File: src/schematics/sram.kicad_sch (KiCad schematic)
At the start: 4 parts

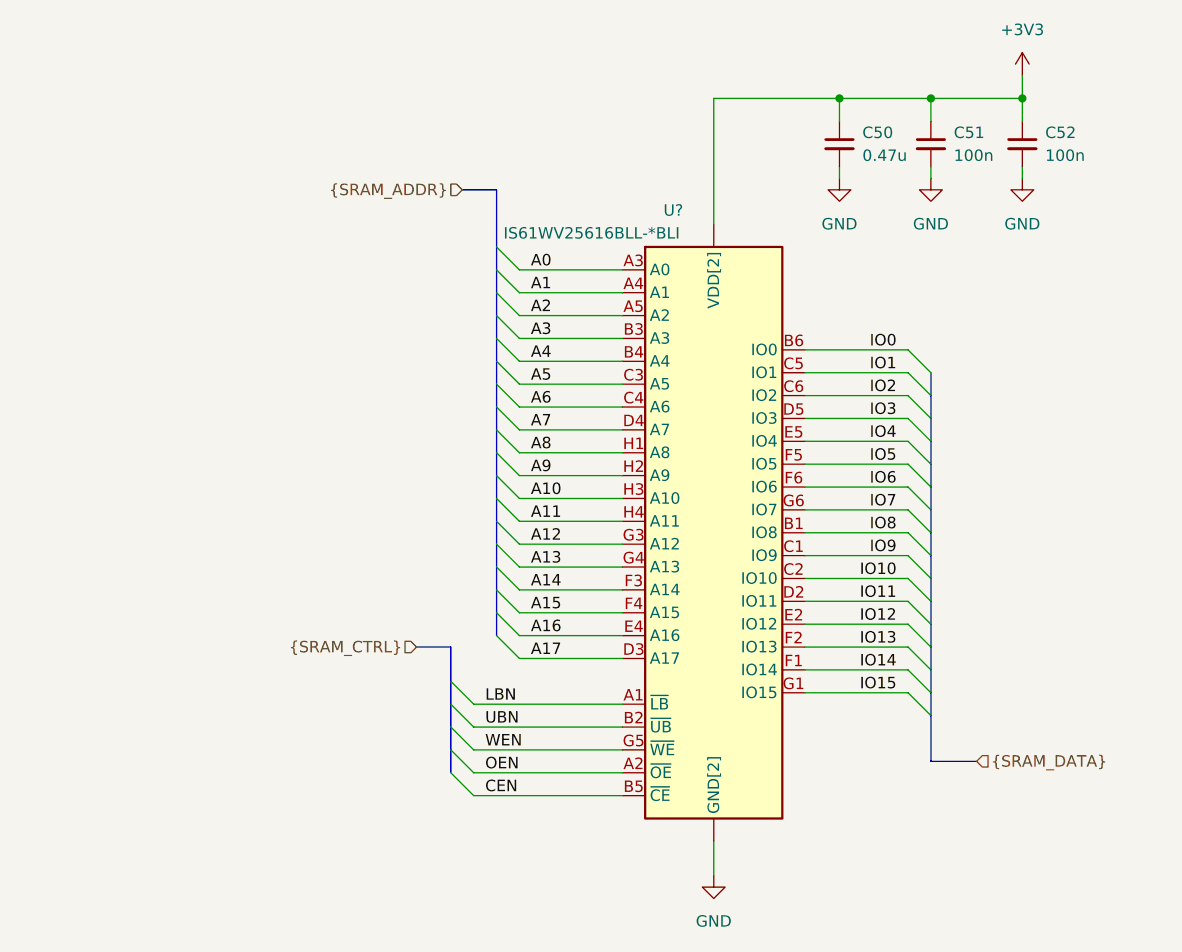
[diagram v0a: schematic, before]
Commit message: Adds the clock oscillator
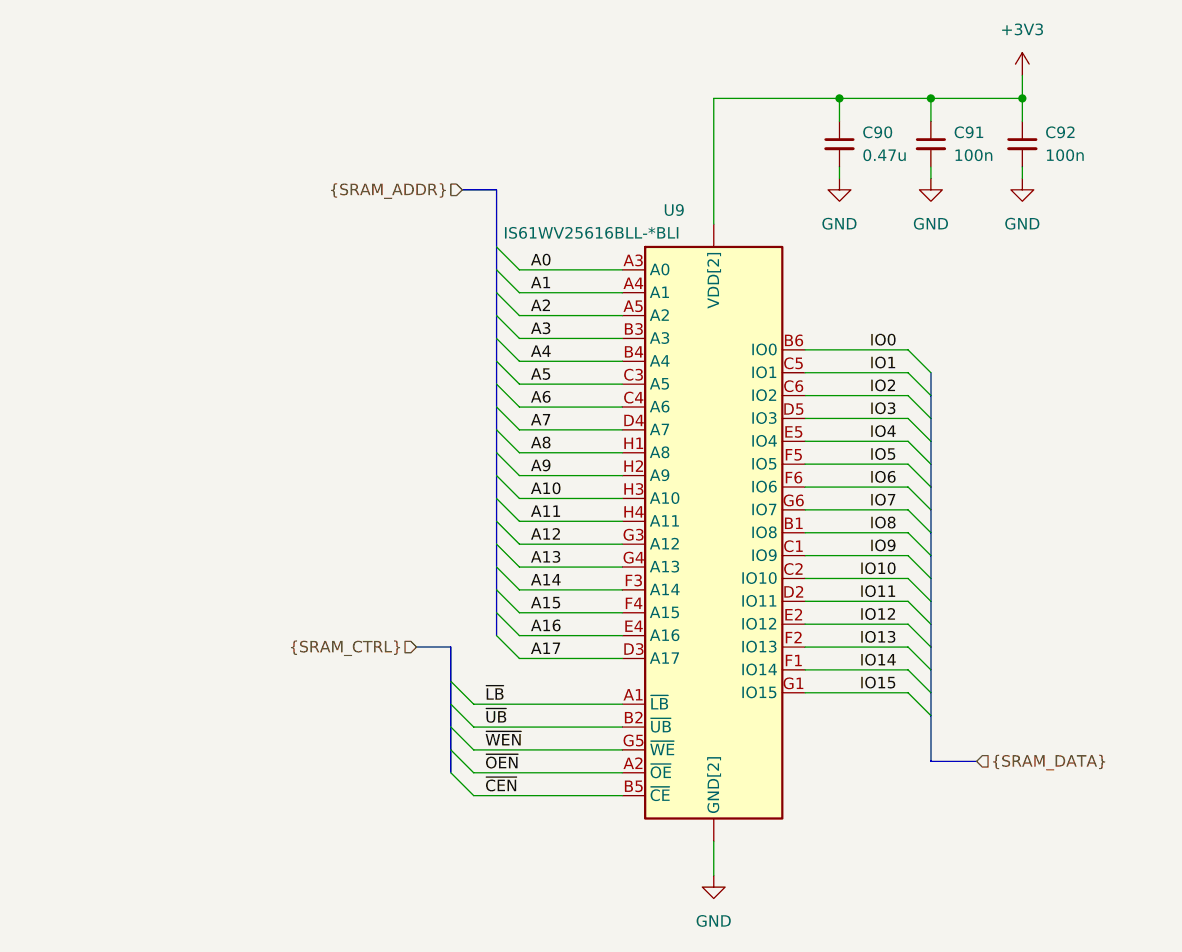
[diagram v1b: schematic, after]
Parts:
- gave numbers to parts that had none: 1
- renumbered C50 to C90, C51 to C91, C52 to C92
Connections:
- net CEN renamed ~{CEN}
- net LBN renamed ~{LB}
- net OEN renamed ~{OEN}
- net UBN renamed ~{UB}
- net WEN renamed ~{WEN}
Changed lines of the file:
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@@
 		)
 	)
-	(label "CEN"
+	(label "~{CEN}"
 		(at 127 125.73 0)
 		(fields_autoplaced yes)
@@
 		)
 	)
-	(label "UBN"
+	(label "~{UB}"
 		(at 127 118.11 0)
 		(fields_autoplaced yes)
@@
 		)
 	)
-	(label "WEN"
+	(label "~{WEN}"
 		(at 127 120.65 0)
 		(fields_autoplaced yes)
@@
 		)
 	)
-	(label "LBN"
+	(label "~{LB}"
 		(at 127 115.57 0)
 		(fields_autoplaced yes)
@@
 		)
 	)
-	(label "OEN"
+	(label "~{OEN}"
 		(at 127 123.19 0)
 		(fields_autoplaced yes)
@@
 		(dnp no)
 		(fields_autoplaced yes)
-		(property "Reference" "#PWR?"
+		(property "Reference" "#PWR094"
 			(at 152.4 140.97 0)
 			(effects
@@
 			(project "ecap5-bsom"
 				(path "/c5fd18a3-9aa0-4151-b6e0-94da3d606686/492906df-f838-4d8b-b74b-2c5ce24fa298"
-					(reference "#PWR?")
+					(reference "#PWR094")
 					(unit 1)
 				)
@@
 		(dnp no)
 		(fields_autoplaced yes)
-		(property "Reference" "C50"
+		(property "Reference" "C90"
 			(at 168.91 52.0762 0)
 			(effects
@@
 			(project "ecap5-bsom"
 				(path "/c5fd18a3-9aa0-4151-b6e0-94da3d606686/492906df-f838-4d8b-b74b-2c5ce24fa298"
-					(reference "C50")
+					(reference "C90")
 					(unit 1)
 				)
@@
 		(dnp no)
 		(fields_autoplaced yes)
-		(property "Reference" "C51"
+		(property "Reference" "C91"
 			(at 179.07 52.0762 0)
 			(effects
@@
 			(project "ecap5-bsom"
 				(path "/c5fd18a3-9aa0-4151-b6e0-94da3d606686/492906df-f838-4d8b-b74b-2c5ce24fa298"
-					(reference "C51")
+					(reference "C91")
 					(unit 1)
 				)
@@
 		(dnp no)
 		(fields_autoplaced yes)
-		(property "Reference" "#PWR055"
+		(property "Reference" "#PWR093"
 			(at 186.69 63.5 0)
 			(effects
@@
 			(project "ecap5-bsom"
 				(path "/c5fd18a3-9aa0-4151-b6e0-94da3d606686/492906df-f838-4d8b-b74b-2c5ce24fa298"
-					(reference "#PWR055")
+					(reference "#PWR093")
 					(unit 1)
 				)
@@
 		(dnp no)
 		(fields_autoplaced yes)
-		(property "Reference" "C52"
+		(property "Reference" "C92"
 			(at 189.23 52.0762 0)
 			(effects
@@
 			(project "ecap5-bsom"
 				(path "/c5fd18a3-9aa0-4151-b6e0-94da3d606686/492906df-f838-4d8b-b74b-2c5ce24fa298"
-					(reference "C52")
+					(reference "C92")
 					(unit 1)
 				)
@@
 		(dnp no)
 		(fields_autoplaced yes)
-		(property "Reference" "#PWR?"
+		(property "Reference" "#PWR090"
 			(at 186.69 49.53 0)
 			(effects
@@
 			(project "ecap5-bsom"
 				(path "/c5fd18a3-9aa0-4151-b6e0-94da3d606686/492906df-f838-4d8b-b74b-2c5ce24fa298"
-					(reference "#PWR?")
+					(reference "#PWR090")
 					(unit 1)
 				)
@@
 		(on_board yes)
 		(dnp no)
-		(property "Reference" "U?"
+		(property "Reference" "U9"
 			(at 146.812 60.706 0)
 			(effects
@@
 			(project "ecap5-bsom"
 				(path "/c5fd18a3-9aa0-4151-b6e0-94da3d606686/492906df-f838-4d8b-b74b-2c5ce24fa298"
-					(reference "U?")
+					(reference "U9")
 					(unit 1)
 				)
@@
 		(dnp no)
 		(fields_autoplaced yes)
-		(property "Reference" "#PWR053"
+		(property "Reference" "#PWR091"
 			(at 166.37 63.5 0)
 			(effects
@@
 			(project "ecap5-bsom"
 				(path "/c5fd18a3-9aa0-4151-b6e0-94da3d606686/492906df-f838-4d8b-b74b-2c5ce24fa298"
-					(reference "#PWR053")
+					(reference "#PWR091")
 					(unit 1)
 				)
@@
 		(dnp no)
 		(fields_autoplaced yes)
-		(property "Reference" "#PWR054"
+		(property "Reference" "#PWR092"
 			(at 176.53 63.5 0)
 			(effects
@@
 			(project "ecap5-bsom"
 				(path "/c5fd18a3-9aa0-4151-b6e0-94da3d606686/492906df-f838-4d8b-b74b-2c5ce24fa298"
-					(reference "#PWR054")
+					(reference "#PWR092")
 					(unit 1)
 				)

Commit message: Adds bus aliases
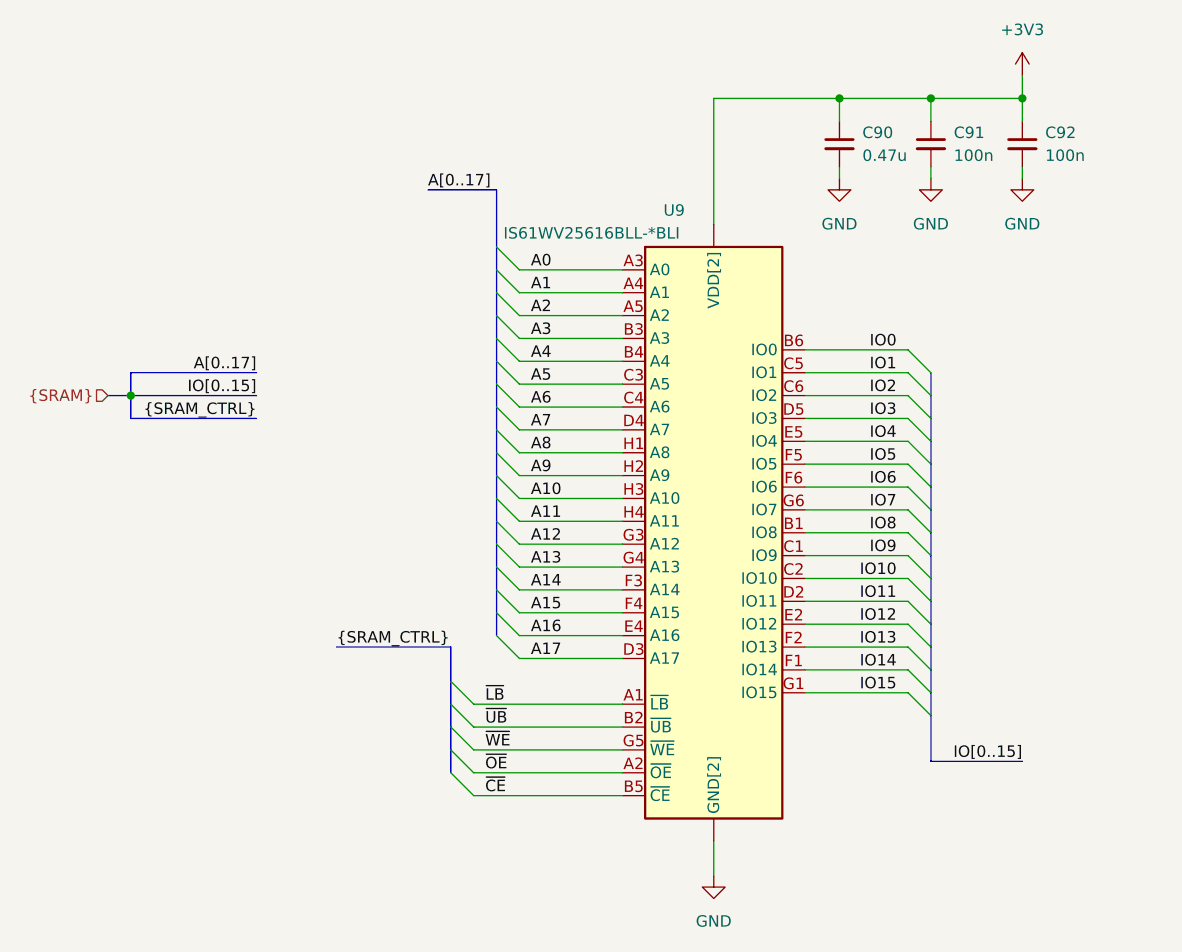
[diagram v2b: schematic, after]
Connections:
- net ~{CEN} renamed ~{CE}
- net ~{OEN} renamed ~{OE}
- net ~{WEN} renamed ~{WE}
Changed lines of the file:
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@@
 		(comment 3 "${Part Number}")
+	)
+	(bus_alias "SRAM"
+		(members "{SRAM_CTRL}" "A[0..17]" "IO[0..15]")
+	)
+	(bus_alias "SRAM_CTRL"
+		(members "~{LB}" "~{UB}" "~{WE}" "~{OE}" "~{CE}")
 	)
 	(junction
@@
 		(color 0 0 0 0)
 	)
+	(junction
+		(at 87.63 81.28)
+		(diameter 0)
+		(color 0 0 0 0)
+	)
 	(bus_entry
 		(at 128.27 100.33)
@@
 	(bus
 		(pts
+			(xy 120.65 58.42) (xy 128.27 58.42)
+		)
+		(stroke
+			(width 0)
+			(type default)
+		)
+	)
+	(bus
+		(pts
 			(xy 128.27 102.87) (xy 128.27 100.33)
 		)
@@
 		)
 	)
+	(bus
+		(pts
+			(xy 101.6 83.82) (xy 87.63 83.82)
+		)
+		(stroke
+			(width 0)
+			(type default)
+		)
+	)
 	(wire
 		(pts
@@
 		)
 	)
+	(bus
+		(pts
+			(xy 110.49 109.22) (xy 123.19 109.22)
+		)
+		(stroke
+			(width 0)
+			(type default)
+		)
+	)
 	(wire
 		(pts
@@
 		)
 	)
+	(bus
+		(pts
+			(xy 87.63 81.28) (xy 101.6 81.28)
+		)
+		(stroke
+			(width 0)
+			(type default)
+		)
+	)
 	(wire
 		(pts
@@
 	(bus
 		(pts
+			(xy 85.09 81.28) (xy 87.63 81.28)
+		)
+		(stroke
+			(width 0)
+			(type default)
+		)
+	)
+	(bus
+		(pts
 			(xy 176.53 109.22) (xy 176.53 106.68)
 		)
@@
 	(bus
 		(pts
-			(xy 124.46 58.42) (xy 128.27 58.42)
+			(xy 87.63 81.28) (xy 87.63 83.82)
 		)
 		(stroke
@@
 		)
 	)
+	(bus
+		(pts
+			(xy 87.63 78.74) (xy 101.6 78.74)
+		)
+		(stroke
+			(width 0)
+			(type default)
+		)
+	)
 	(wire
 		(pts
@@
 	(bus
 		(pts
+			(xy 87.63 81.28) (xy 87.63 78.74)
+		)
+		(stroke
+			(width 0)
+			(type default)
+		)
+	)
+	(bus
+		(pts
 			(xy 123.19 118.11) (xy 123.19 120.65)
 		)
@@
 		)
 	)
-	(bus
-		(pts
-			(xy 119.38 109.22) (xy 123.19 109.22)
-		)
-		(stroke
-			(width 0)
-			(type default)
-		)
-	)
 	(wire
 		(pts
@@
 	(bus
 		(pts
-			(xy 176.53 121.92) (xy 181.61 121.92)
+			(xy 176.53 121.92) (xy 186.69 121.92)
 		)
 		(stroke
@@
 		)
 	)
+	(label "IO[0..15]"
+		(at 101.6 81.28 180)
+		(fields_autoplaced yes)
+		(effects
+			(font
+				(size 1.27 1.27)
+			)
+			(justify right bottom)
+		)
+	)
 	(label "A10"
 		(at 132.08 92.71 0)
@@
 		)
 	)
-	(label "~{CEN}"
+	(label "~{CE}"
 		(at 127 125.73 0)
 		(fields_autoplaced yes)
@@
 			)
 			(justify left bottom)
+		)
+	)
+	(label "A[0..17]"
+		(at 101.6 78.74 180)
+		(fields_autoplaced yes)
+		(effects
+			(font
+				(size 1.27 1.27)
+			)
+			(justify right bottom)
 		)
 	)
@@
 		)
 	)
-	(label "~{WEN}"
+	(label "A[0..17]"
+		(at 120.65 58.42 0)
+		(fields_autoplaced yes)
+		(effects
+			(font
+				(size 1.27 1.27)
+			)
+			(justify left bottom)
+		)
+	)
+	(label "{SRAM_CTRL}"
+		(at 101.6 83.82 180)
+		(fields_autoplaced yes)
+		(effects
+			(font
+				(size 1.27 1.27)
+			)
+			(justify right bottom)
+		)
+	)
+	(label "~{WE}"
 		(at 127 120.65 0)
 		(fields_autoplaced yes)
@@
 		)
 	)
+	(label "IO[0..15]"
+		(at 186.69 121.92 180)
+		(fields_autoplaced yes)
+		(effects
+			(font
+				(size 1.27 1.27)
+			)
+			(justify right bottom)
+		)
+	)
 	(label "A12"
 		(at 132.08 97.79 0)
@@
 		)
 	)
-	(label "~{OEN}"
+	(label "~{OE}"
 		(at 127 123.19 0)
 		(fields_autoplaced yes)
@@
 		)
 	)
-	(hierarchical_label "{SRAM_ADDR}"
+	(label "{SRAM_CTRL}"
+		(at 110.49 109.22 0)
+		(fields_autoplaced yes)
+		(effects
+			(font
+				(size 1.27 1.27)
+			)
+			(justify left bottom)
+		)
+	)
+	(hierarchical_label "{SRAM}"
 		(shape input)
-		(at 124.46 58.42 180)
-		(fields_autoplaced yes)
-		(effects
-			(font
-				(size 1.27 1.27)
-			)
-			(justify right)
-		)
-	)
-	(hierarchical_label "{SRAM_DATA}"
-		(shape input)
-		(at 181.61 121.92 0)
-		(fields_autoplaced yes)
-		(effects
-			(font
-				(size 1.27 1.27)
-			)
-			(justify left)
-		)
-	)
-	(hierarchical_label "{SRAM_CTRL}"
-		(shape input)
-		(at 119.38 109.22 180)
-		(fields_autoplaced yes)
-		(effects
+		(at 85.09 81.28 180)
+		(fields_autoplaced yes)
+		(effects

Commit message: Fix some ERC issues
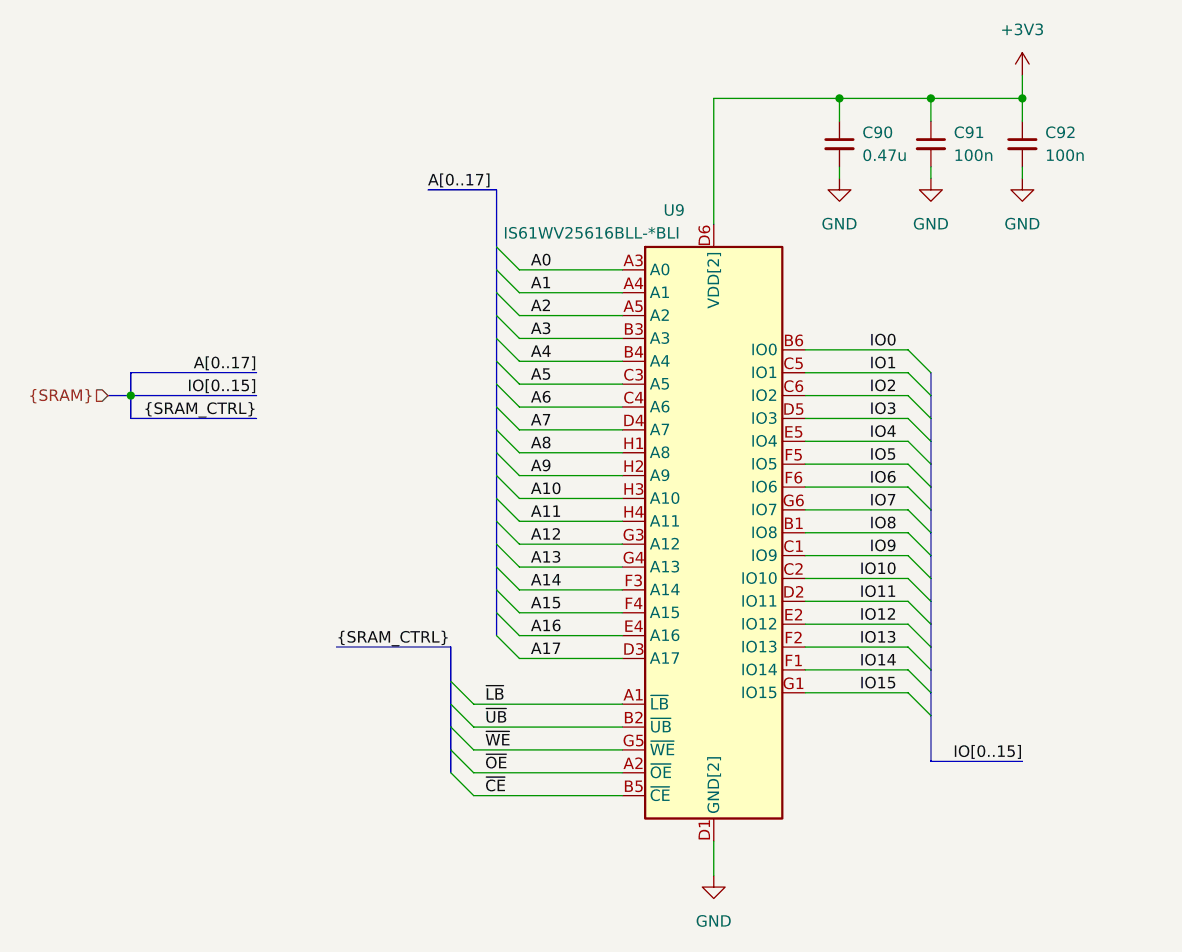
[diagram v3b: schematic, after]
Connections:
- net +3V3: no longer U9. (VDD[2])
- net GND: no longer U9. (VDD[2])
- net NC: no longer names the net of U9. (NC[5]), U9.A6 (NC), U9.E3 (NC), U9.G2 (NC), U9.H1 (NC), U9.H6 (NC)
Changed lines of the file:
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@@
 		(pin "C1"
-		)
-		(pin ""
 		)
 		(pin "F5"
 		)
-		(pin ""
-		)
 		(pin "D3"

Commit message: Fixes bus aliases
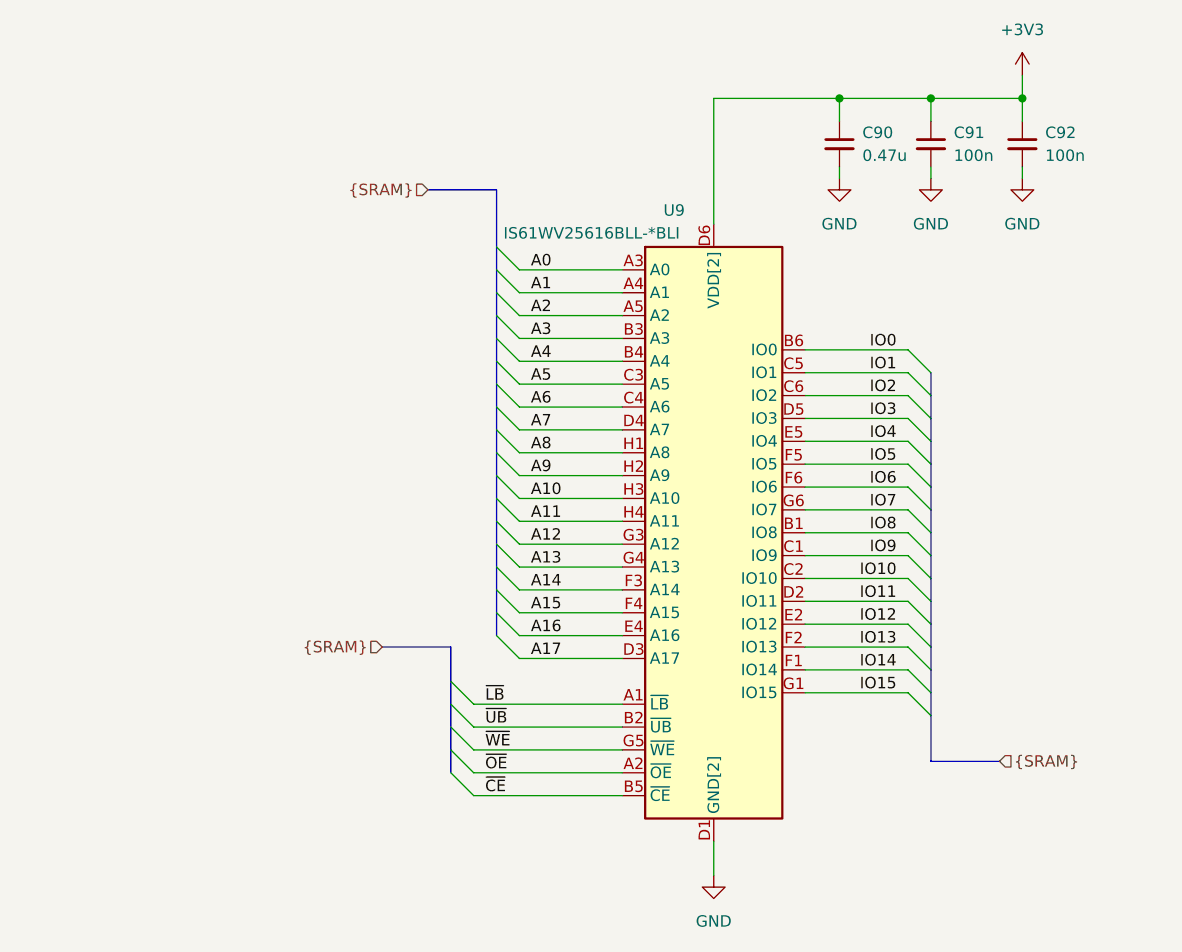
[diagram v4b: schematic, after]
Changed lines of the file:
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@@
 	)
 	(bus_alias "SRAM"
-		(members "{SRAM_CTRL}" "A[0..17]" "IO[0..15]")
-	)
-	(bus_alias "SRAM_CTRL"
-		(members "~{LB}" "~{UB}" "~{WE}" "~{OE}" "~{CE}")
+		(members "~{LB}" "~{UB}" "~{WE}" "~{OE}" "~{CE}" "A[0..17]" "IO[0..15]")
 	)
 	(junction
@@
 		(color 0 0 0 0)
 	)
-	(junction
-		(at 87.63 81.28)
-		(diameter 0)
-		(color 0 0 0 0)
-	)
 	(bus_entry
 		(at 128.27 100.33)
@@
 		)
 	)
-	(bus
-		(pts
-			(xy 101.6 83.82) (xy 87.63 83.82)
-		)
-		(stroke
-			(width 0)
-			(type default)
-		)
-	)
 	(wire
 		(pts
@@
 	(bus
 		(pts
-			(xy 110.49 109.22) (xy 123.19 109.22)
+			(xy 115.57 109.22) (xy 123.19 109.22)
 		)
 		(stroke
@@
 		)
 	)
-	(bus
-		(pts
-			(xy 87.63 81.28) (xy 101.6 81.28)
-		)
-		(stroke
-			(width 0)
-			(type default)
-		)
-	)
 	(wire
 		(pts
@@
 	(bus
 		(pts
-			(xy 85.09 81.28) (xy 87.63 81.28)
-		)
-		(stroke
-			(width 0)
-			(type default)
-		)
-	)
-	(bus
-		(pts
 			(xy 176.53 109.22) (xy 176.53 106.68)
 		)
@@
 		)
 	)
-	(bus
-		(pts
-			(xy 87.63 81.28) (xy 87.63 83.82)
-		)
-		(stroke
-			(width 0)
-			(type default)
-		)
-	)
 	(wire
 		(pts
@@
 		)
 	)
-	(bus
-		(pts
-			(xy 87.63 78.74) (xy 101.6 78.74)
-		)
-		(stroke
-			(width 0)
-			(type default)
-		)
-	)
 	(wire
 		(pts
@@
 	(bus
 		(pts
-			(xy 87.63 81.28) (xy 87.63 78.74)
-		)
-		(stroke
-			(width 0)
-			(type default)
-		)
-	)
-	(bus
-		(pts
 			(xy 123.19 118.11) (xy 123.19 120.65)
 		)
@@
 	(bus
 		(pts
-			(xy 176.53 121.92) (xy 186.69 121.92)
+			(xy 176.53 121.92) (xy 184.15 121.92)
 		)
 		(stroke
@@
 		)
 	)
-	(label "IO[0..15]"
-		(at 101.6 81.28 180)
-		(fields_autoplaced yes)
-		(effects
-			(font
-				(size 1.27 1.27)
-			)
-			(justify right bottom)
-		)
-	)
 	(label "A10"
 		(at 132.08 92.71 0)
@@
 		)
 	)
-	(label "A[0..17]"
-		(at 101.6 78.74 180)
-		(fields_autoplaced yes)
-		(effects
-			(font
-				(size 1.27 1.27)
-			)
-			(justify right bottom)
-		)
-	)
 	(label "A0"
 		(at 132.08 67.31 0)
@@
 		)
 	)
-	(label "A[0..17]"
-		(at 120.65 58.42 0)
-		(fields_autoplaced yes)
-		(effects
-			(font
-				(size 1.27 1.27)
-			)
-			(justify left bottom)
-		)
-	)
-	(label "{SRAM_CTRL}"
-		(at 101.6 83.82 180)
-		(fields_autoplaced yes)
-		(effects
-			(font
-				(size 1.27 1.27)
-			)
-			(justify right bottom)
-		)
-	)
 	(label "~{WE}"
 		(at 127 120.65 0)
@@
 		)
 	)
-	(label "IO[0..15]"
-		(at 186.69 121.92 180)
-		(fields_autoplaced yes)
-		(effects
-			(font
-				(size 1.27 1.27)
-			)
-			(justify right bottom)
-		)
-	)
 	(label "A12"
 		(at 132.08 97.79 0)
@@
 		)
 	)
-	(label "{SRAM_CTRL}"
-		(at 110.49 109.22 0)
-		(fields_autoplaced yes)
-		(effects
-			(font
-				(size 1.27 1.27)
-			)
-			(justify left bottom)
-		)
-	)
 	(hierarchical_label "{SRAM}"
 		(shape input)
-		(at 85.09 81.28 180)
-		(fields_autoplaced yes)
-		(effects
+		(at 115.57 109.22 180)
+		(fields_autoplaced yes)
+		(effects
+			(font
+				(size 1.27 1.27)
+			)
+			(justify right)
+		)
+	)
+	(hierarchical_label "{SRAM}"
+		(shape input)
+		(at 184.15 121.92 0)
+		(fields_autoplaced yes)
+		(effects
+			(font
+				(size 1.27 1.27)
+			)
+			(justify left)
+		)
+	)
+	(hierarchical_label "{SRAM}"
+		(shape input)
+		(at 120.65 58.42 180)
+		(fields_autoplaced yes)
+		(effects
